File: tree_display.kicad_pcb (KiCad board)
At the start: 2 copper layers, 61 x 70.2 mm, 41 parts

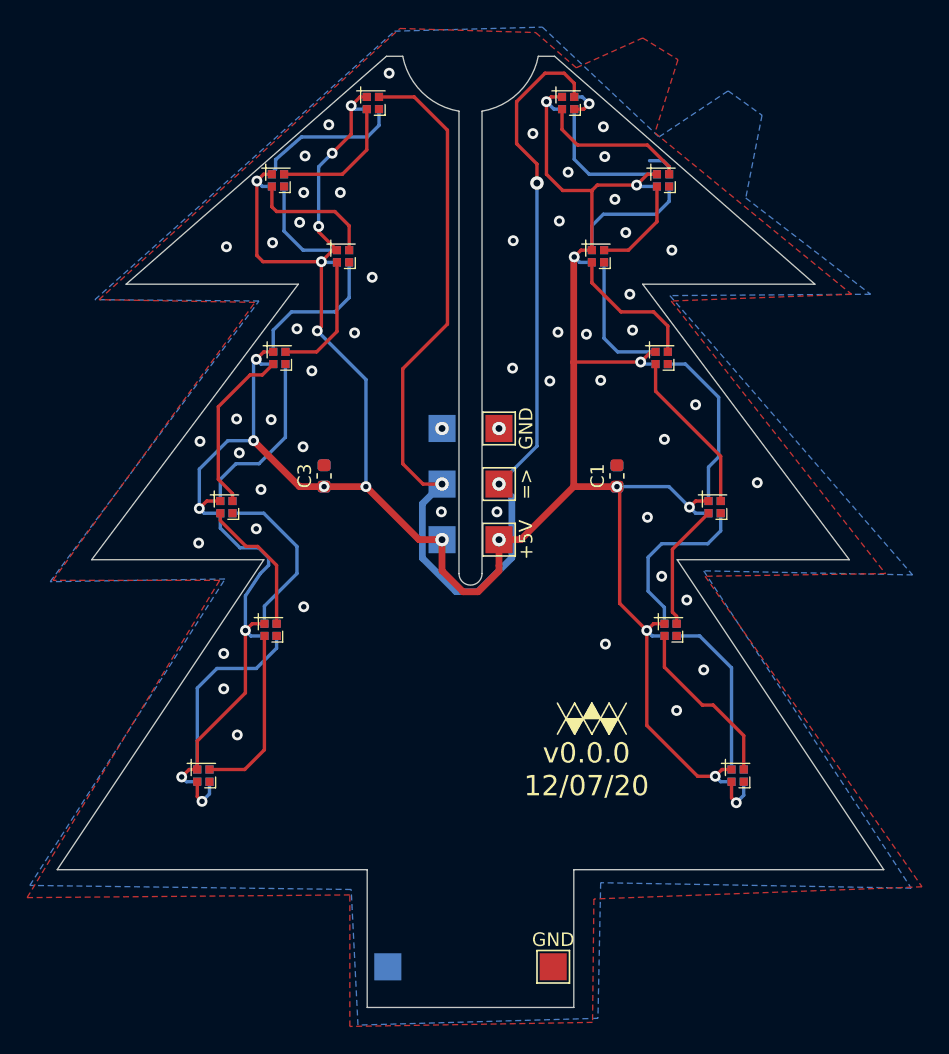
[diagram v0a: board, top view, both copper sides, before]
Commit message: Move right side LEDs to back to break up pattern
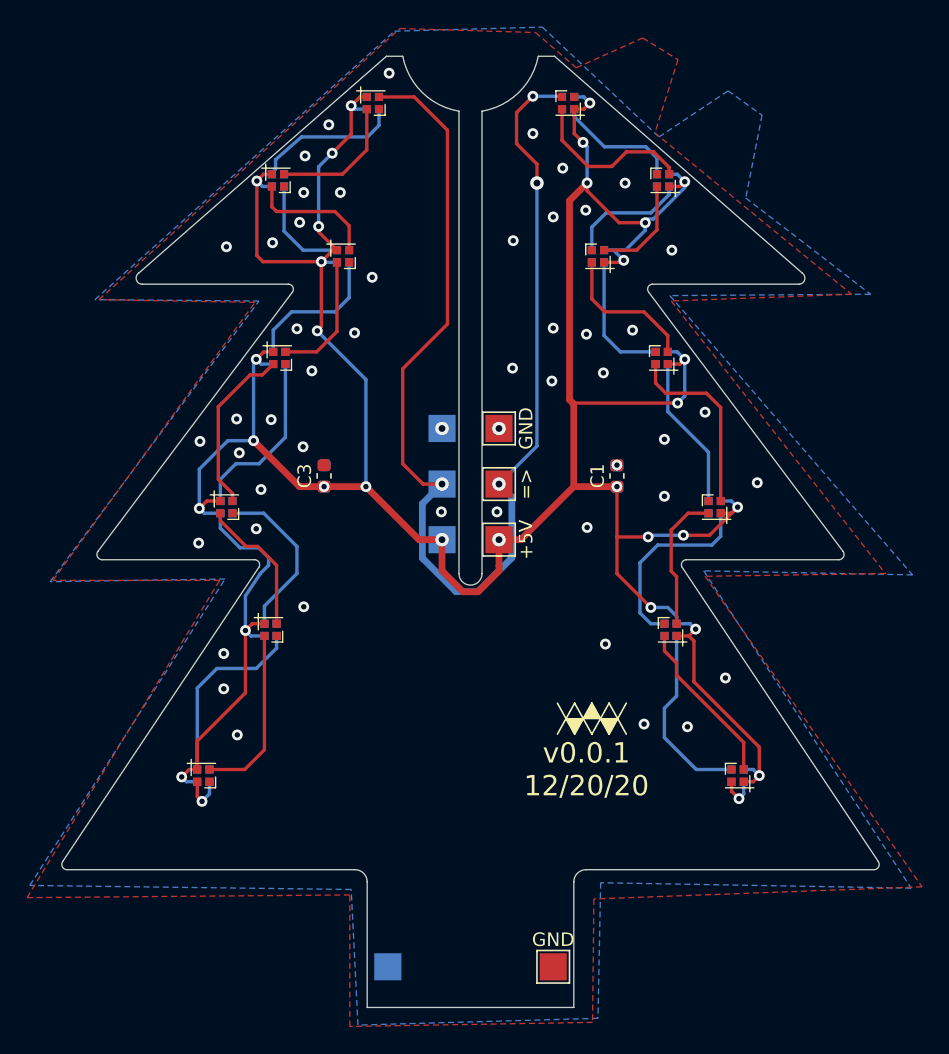
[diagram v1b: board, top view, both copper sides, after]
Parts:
- D1, D2, D3, D4, D5, D6, D7: moved to B.Cu
- D10, D11, D12, D13, D14, D8, D9: moved to F.Cu
- turned D1 to 180 degrees
- turned D10 to 180 degrees
- turned D11 to 180 degrees
- turned D12 to 180 degrees
- turned D13 to 180 degrees
- turned D14 to 180 degrees
- turned D2 to 180 degrees
- turned D3 to 180 degrees
- turned D4 to 180 degrees
- turned D5 to 180 degrees
- turned D6 to 180 degrees
- turned D7 to 180 degrees
- turned D8 to 180 degrees
- turned D9 to 180 degrees
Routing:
- net +5V: track 225.9 -> 245.1 mm, vias 23 -> 30
- net Net-(D5-Pad1): track 9.38 -> 14.3 mm
- net GND: track 4.76 -> 0.00 mm, vias 54 -> 51
- net DIN: track 92.5 -> 89.2 mm, vias 3 -> 4
- net Net-(D10-Pad3): track 12.9 -> 10.3 mm
- net Net-(D13-Pad1): track 10.3 -> 12.4 mm
- net Net-(D1-Pad1): track 11.1 -> 9.11 mm
- net Net-(D2-Pad1): track 7.37 -> 8.99 mm
- net Net-(D12-Pad1): track 9.35 -> 7.72 mm
- net Net-(D10-Pad1): track 12.7 -> 13.8 mm
- net Net-(D6-Pad1): track 12.7 -> 13.8 mm
- net Net-(D11-Pad1): track 9.81 -> 10.6 mm
- net Net-(D4-Pad1): track 12.1 -> 11.3 mm
- net Net-(D3-Pad1): track 10.3 -> 9.70 mm
- net Net-(D7-Pad1): track 3.47 -> 2.87 mm
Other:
- board size 61 x 70.2 mm -> 60.3 x 70.2 mm
- board text added: "v0.0.1 12/20/20"
- board text removed: "v0.0.0 12/07/20"
